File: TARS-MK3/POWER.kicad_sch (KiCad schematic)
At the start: 58 parts, among them J1 Conn_02x12_Odd_Even, J2 Conn_02x12_Odd_Even, J3 Conn_02x12_Odd_Even, J4 Conn_02x12_Odd_Even, J5 AVRISP, U1 LK112M33TR, U2 ATmega328P-A, U3 D36V50F6, U4 D36V50F6, U5 D36V28F9, U6 D36V28F3, U7 D24V50F5, Y1 8Mhz

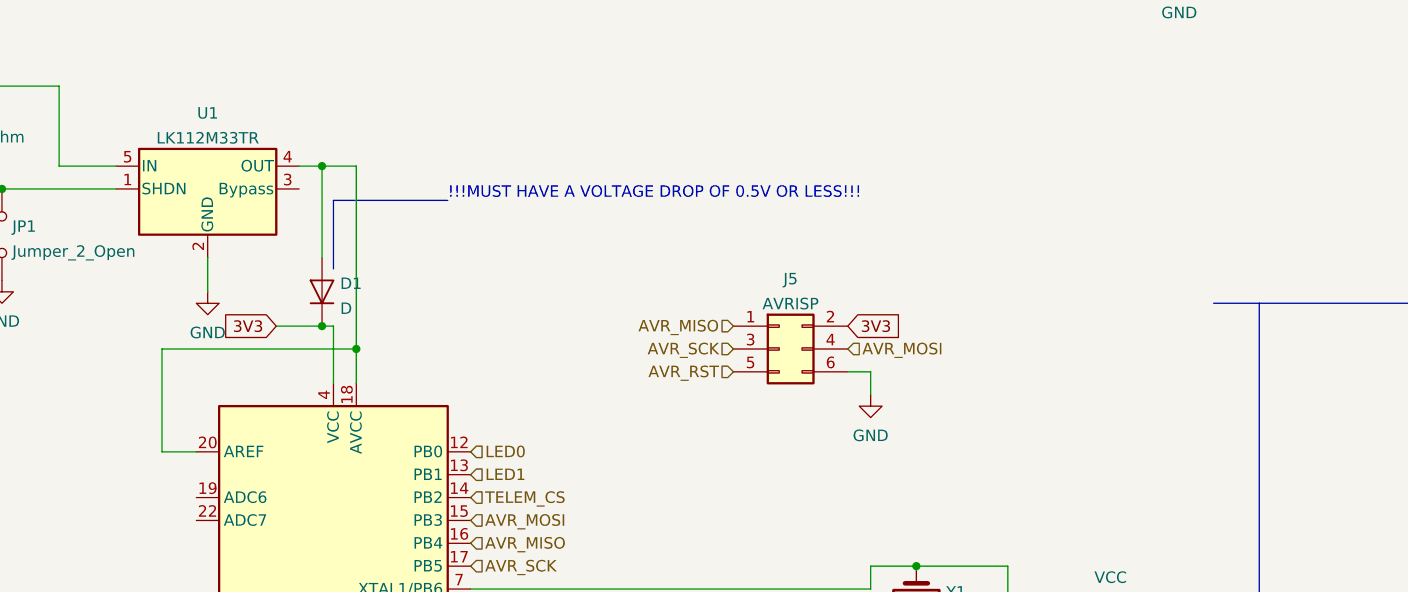
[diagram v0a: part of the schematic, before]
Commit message: Put regulators on PMB and began layout
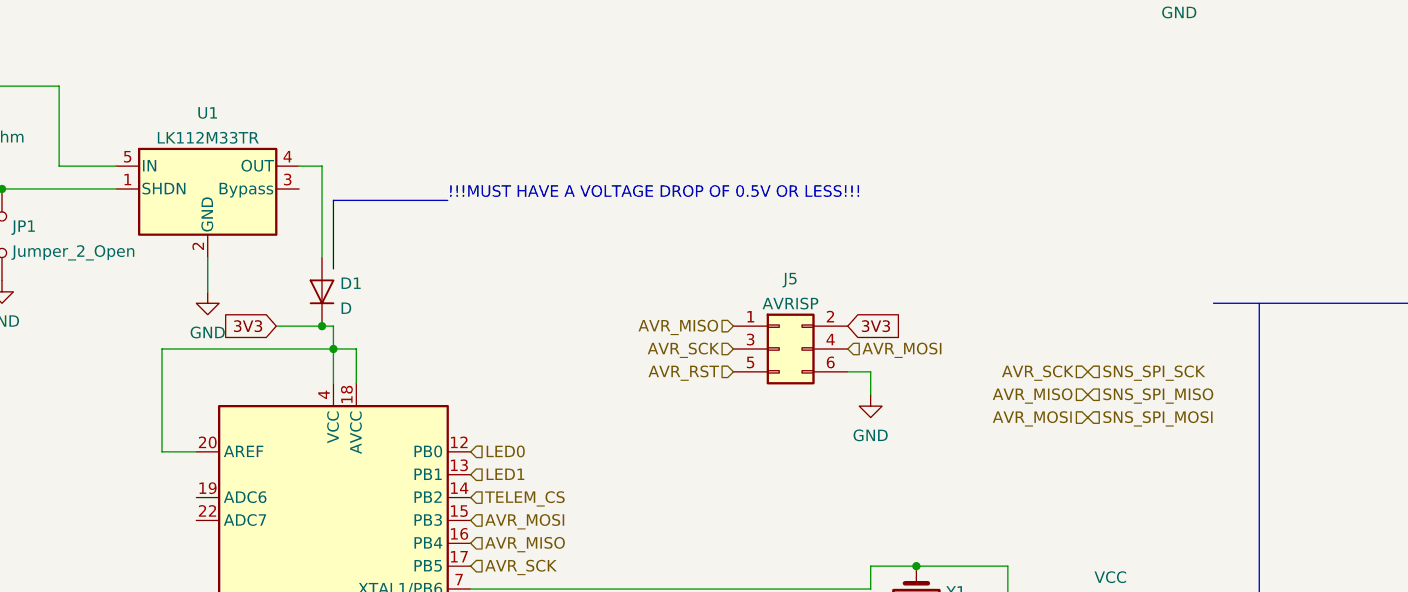
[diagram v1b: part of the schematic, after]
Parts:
- D5: footprint Diode_SMD:D_0603_1608Metric -> Diode_SMD:D_0805_2012Metric
- R18: footprint Resistor_SMD:R_0201_0603Metric -> Resistor_SMD:R_0805_2012Metric
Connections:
- net 3V3: now also U2.18 (AVCC), U2.20 (AREF)
- net at D1.2 (A), U1.4 (OUT): no longer U2.18 (AVCC), U2.20 (AREF)
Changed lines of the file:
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@@
   (junction (at 41.91 176.53) (diameter 0) (color 0 0 0 0)
   )
+  (junction (at 59.69 33.02) (diameter 0) (color 0 0 0 0)
+  )
   (junction (at -33.02 105.41) (diameter 0) (color 0 0 0 0)
   )
@@
   (junction (at 124.46 57.15) (diameter 0) (color 0 0 0 0)
   )
-  (junction (at 58.42 12.7) (diameter 0) (color 0 0 0 0)
-  )
   (junction (at 74.93 184.15) (diameter 0) (color 0 0 0 0)
   )
@@
   )
   (junction (at 58.42 30.48) (diameter 0) (color 0 0 0 0)
-  )
-  (junction (at 62.23 33.02) (diameter 0) (color 0 0 0 0)
   )
   (junction (at 7.62 3.81) (diameter 0) (color 0 0 0 0)
@@
     (stroke (width 0) (type default) (color 0 0 0 0))
   )
-  (wire (pts (xy 62.23 12.7) (xy 62.23 33.02))
-    (stroke (width 0) (type default) (color 0 0 0 0))
-  )
   (wire (pts (xy 69.85 184.15) (xy 69.85 186.69))
     (stroke (width 0) (type default) (color 0 0 0 0))
@@
     (stroke (width 0) (type default) (color 0 0 0 0))
   )
-  (wire (pts (xy 62.23 33.02) (xy 40.64 33.02))
-    (stroke (width 0) (type default) (color 0 0 0 0))
-  )
   (wire (pts (xy 7.62 35.56) (xy 7.62 38.1))
     (stroke (width 0) (type default) (color 0 0 0 0))
@@
     (stroke (width 0) (type default) (color 0 0 0 0))
   )
+  (wire (pts (xy 40.64 33.02) (xy 59.69 33.02))
+    (stroke (width 0) (type default) (color 0 0 0 0))
+  )
   (wire (pts (xy 74.93 90.17) (xy 80.01 90.17))
     (stroke (width 0) (type default) (color 0 0 0 0))
@@
     (stroke (width 0) (type default) (color 0 0 0 0))
   )
-  (wire (pts (xy 59.69 30.48) (xy 59.69 36.83))
+  (wire (pts (xy 59.69 30.48) (xy 59.69 33.02))
     (stroke (width 0) (type default) (color 0 0 0 0))
   )
@@
     (stroke (width 0) (type default) (color 0 0 0 0))
   )
-  (wire (pts (xy 58.42 12.7) (xy 62.23 12.7))
-    (stroke (width 0) (type default) (color 0 0 0 0))
-  )
   (wire (pts (xy -31.75 148.59) (xy -31.75 151.13))
     (stroke (width 0) (type default) (color 0 0 0 0))
@@
     (stroke (width 0) (type default) (color 0 0 0 0))
   )
+  (wire (pts (xy 59.69 33.02) (xy 62.23 33.02))
+    (stroke (width 0) (type default) (color 0 0 0 0))
+  )
   (wire (pts (xy 121.92 72.39) (xy 121.92 73.66))
     (stroke (width 0) (type default) (color 0 0 0 0))
@@
   )
   (wire (pts (xy 92.71 171.45) (xy 90.17 171.45))
+    (stroke (width 0) (type default) (color 0 0 0 0))
+  )
+  (wire (pts (xy 59.69 33.02) (xy 59.69 36.83))
     (stroke (width 0) (type default) (color 0 0 0 0))
   )
@@
     (effects (font (size 1.27 1.27)) (justify left))
   )
+  (hierarchical_label "AVR_MOSI" (shape input) (at 143.51 40.64 180)
+    (effects (font (size 1.27 1.27)) (justify right))
+  )
   (hierarchical_label "B2B_GPIO_21" (shape input) (at 398.78 257.81 0)
     (effects (font (size 1.27 1.27)) (justify left))
@@
     (effects (font (size 1.27 1.27)) (justify left))
   )
+  (hierarchical_label "SNS_SPI_MISO" (shape input) (at 143.51 38.1 0)
+    (effects (font (size 1.27 1.27)) (justify left))
+  )
   (hierarchical_label "TELEM_CS" (shape input) (at 74.93 49.53 0)
     (effects (font (size 1.27 1.27)) (justify left))
@@
     (effects (font (size 1.27 1.27)) (justify left))
   )
+  (hierarchical_label "SNS_SPI_MOSI" (shape input) (at 143.51 40.64 0)
+    (effects (font (size 1.27 1.27)) (justify left))
+  )
   (hierarchical_label "POWER_RESET" (shape input) (at 309.88 285.75 180)
     (effects (font (size 1.27 1.27)) (justify right))
@@
     (effects (font (size 1.27 1.27)) (justify right))
   )
+  (hierarchical_label "SNS_SPI_SCK" (shape input) (at 143.51 35.56 0)
+    (effects (font (size 1.27 1.27)) (justify left))
+  )
   (hierarchical_label "TELEM_RST" (shape input) (at 309.88 280.67 180)
     (effects (font (size 1.27 1.27)) (justify right))
@@
     (effects (font (size 1.27 1.27)) (justify left))
   )
+  (hierarchical_label "AVR_SCK" (shape input) (at 143.51 35.56 180)
+    (effects (font (size 1.27 1.27)) (justify right))
+  )
   (hierarchical_label "B2B_SPI_SCK" (shape input) (at 322.58 288.29 0)
     (effects (font (size 1.27 1.27)) (justify left))
@@
   (hierarchical_label "B2B_UART_SDI" (shape input) (at 80.01 90.17 0)
     (effects (font (size 1.27 1.27)) (justify left))
+  )
+  (hierarchical_label "AVR_MISO" (shape input) (at 143.51 38.1 180)
+    (effects (font (size 1.27 1.27)) (justify right))
   )
   (hierarchical_label "VBAT_MONITOR" (shape input) (at 74.93 67.31 0)
@@
       (effects (font (size 1.27 1.27)) (justify right))
     )
-    (property "Footprint" "Diode_SMD:D_0603_1608Metric" (id 2) (at 212.09 97.79 0)
+    (property "Footprint" "Diode_SMD:D_0805_2012Metric" (id 2) (at 212.09 97.79 0)
       (effects (font (size 1.27 1.27)) hide)
     )
@@
       (effects (font (size 1.27 1.27)) (justify left))
     )
-    (property "Footprint" "Resistor_SMD:R_0201_0603Metric" (id 2) (at 147.066 68.834 90)
+    (property "Footprint" "Resistor_SMD:R_0805_2012Metric" (id 2) (at 147.066 68.834 90)
       (effects (font (size 1.27 1.27)) hide)
     )
@@
     )
     (path "/5ec3bd07-85f5-47e9-a70f-b13f8032dfa2"
-      (reference "D5") (unit 1) (value "LED") (footprint "Diode_SMD:D_0603_1608Metric")
+      (reference "D5") (unit 1) (value "LED") (footprint "Diode_SMD:D_0805_2012Metric")
     )
     (path "/c422545a-de65-4e06-bd9a-ee5945c74c24"
@@
     )
     (path "/623a95d3-92aa-43fc-bfb7-1927169d4600"
-      (reference "R18") (unit 1) (value "10k") (footprint "Resistor_SMD:R_0201_0603Metric")
+      (reference "R18") (unit 1) (value "10k") (footprint "Resistor_SMD:R_0805_2012Metric")
     )
     (path "/6b57d1f0-e39c-4e10-877e-87d046ef1ca7"

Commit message: updated powerboard footprint
updated powerboard footprint
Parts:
- U3, U4: footprint Pololu_regulators:Pololu_6V -> D36V50F6:D36V50F6-TARS
- U5, U6: footprint Pololu_regulators:Pololu_3V3_5V_9V -> D36V28F3:D36V28F3
- U7: footprint Pololu_regulators:Pololu_3V3_5V_9V -> D24V50F5:D24V50F5
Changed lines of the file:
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@@
     (property "Reference" "U5" (id 0) (at 198.12 135.8605 0))
     (property "Value" "D36V28F9" (id 1) (at 198.12 138.6356 0))
-    (property "Footprint" "Pololu_regulators:Pololu_3V3_5V_9V" (id 2) (at 199.39 158.75 0)
+    (property "Footprint" "D36V28F3:D36V28F3" (id 2) (at 199.39 158.75 0)
       (effects (font (size 1.27 1.27)) hide)
     )
@@
     (property "Reference" "U3" (id 0) (at 76.2 128.2405 0))
     (property "Value" "D36V50F6" (id 1) (at 76.2 131.0156 0))
-    (property "Footprint" "Pololu_regulators:Pololu_6V" (id 2) (at 76.2 130.81 0)
+    (property "Footprint" "D36V50F6:D36V50F6-TARS" (id 2) (at 76.2 130.81 0)
       (effects (font (size 1.27 1.27)) hide)
     )
@@
     (property "Reference" "U7" (id 0) (at 227.33 66.04 0))
     (property "Value" "D24V50F5" (id 1) (at 227.33 68.58 0))
-    (property "Footprint" "Pololu_regulators:Pololu_3V3_5V_9V" (id 2) (at 227.33 71.12 0))
+    (property "Footprint" "D24V50F5:D24V50F5" (id 2) (at 227.33 71.12 0))
     (property "Datasheet" "" (id 3) (at 227.33 72.39 0)
       (effects (font (size 1.27 1.27)) hide)
@@
     (property "Reference" "U4" (id 0) (at 76.2 162.5305 0))
     (property "Value" "D36V50F6" (id 1) (at 76.2 165.3056 0))
-    (property "Footprint" "Pololu_regulators:Pololu_6V" (id 2) (at 76.2 165.1 0)
+    (property "Footprint" "D36V50F6:D36V50F6-TARS" (id 2) (at 76.2 165.1 0)
       (effects (font (size 1.27 1.27)) hide)
     )
@@
     (property "Reference" "U6" (id 0) (at 227.33 36.83 0))
     (property "Value" "D36V28F3" (id 1) (at 227.33 39.37 0))
-    (property "Footprint" "Pololu_regulators:Pololu_3V3_5V_9V" (id 2) (at 213.36 54.61 0)
+    (property "Footprint" "D36V28F3:D36V28F3" (id 2) (at 213.36 54.61 0)
       (effects (font (size 1.27 1.27)) hide)
     )
@@
     )
     (path "/3b87441e-9545-4daa-bf5c-0e30f2dd4c01"
-      (reference "U3") (unit 1) (value "D36V50F6") (footprint "Pololu_regulators:Pololu_6V")
+      (reference "U3") (unit 1) (value "D36V50F6") (footprint "D36V50F6:D36V50F6-TARS")
     )
     (path "/d599ee5f-5c96-4c6d-a4f2-87e98db0087b"
-      (reference "U4") (unit 1) (value "D36V50F6") (footprint "Pololu_regulators:Pololu_6V")
+      (reference "U4") (unit 1) (value "D36V50F6") (footprint "D36V50F6:D36V50F6-TARS")
     )
     (path "/100a73e7-13ce-43bc-8783-1b4a2e371823"
-      (reference "U5") (unit 1) (value "D36V28F9") (footprint "Pololu_regulators:Pololu_3V3_5V_9V")
+      (reference "U5") (unit 1) (value "D36V28F9") (footprint "D36V28F3:D36V28F3")
     )
     (path "/fdff5ae7-e28b-42b9-8347-c09e41256987"
-      (reference "U6") (unit 1) (value "D36V28F3") (footprint "Pololu_regulators:Pololu_3V3_5V_9V")
+      (reference "U6") (unit 1) (value "D36V28F3") (footprint "D36V28F3:D36V28F3")
     )
     (path "/60d76cd4-7135-41b5-bb14-f84115e2b595"
-      (reference "U7") (unit 1) (value "D24V50F5") (footprint "Pololu_regulators:Pololu_3V3_5V_9V")
+      (reference "U7") (unit 1) (value "D24V50F5") (footprint "D24V50F5:D24V50F5")
     )
     (path "/dc0ca2fc-3599-4142-ace0-e48580dd6bc3"

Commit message: finished POWER
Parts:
- removed R11: 200kOhm, Resistor_SMD:R_0805_2012Metric, symbol D24V50F5:R_US
- removed R12: 100kOhm, Resistor_SMD:R_0805_2012Metric, symbol D24V50F5:R_US
- D4: footprint Diode_SMD:D_0603_1608Metric -> LED_SMD:LED_0805_2012Metric
- D5: footprint Diode_SMD:D_0805_2012Metric -> LED_SMD:LED_0805_2012Metric
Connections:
- net B2B_GPIO_21 is gone; now on net 6V_AC_SERVO2: J3.24 (Pin_24), J4.23 (Pin_23)
- net B2B_GPIO_4 is gone; now on net 6V_AC_SERVO1: J1.24 (Pin_24), J2.23 (Pin_23)
- net VCC is gone; now on net 3V3: R18.1
- net 3V3_EN: no longer JP4.2 (B)
- net 6V_AC_SERVO1_EN: no longer JP3.2 (B), U2.10 (PD6)
- net 9V_EN: now also JP4.2 (B)
- new net 6V_AC_SERVO2_EN: JP3.2 (B), U2.10 (PD6)

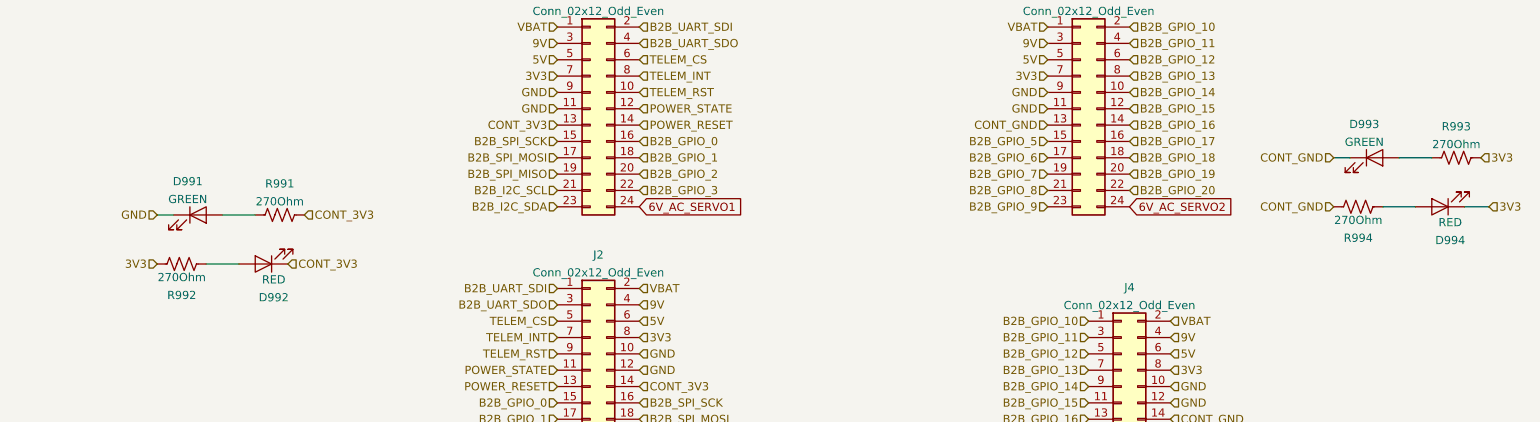
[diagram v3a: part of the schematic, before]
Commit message: Connected continuity check pins correctly on PMB schematic
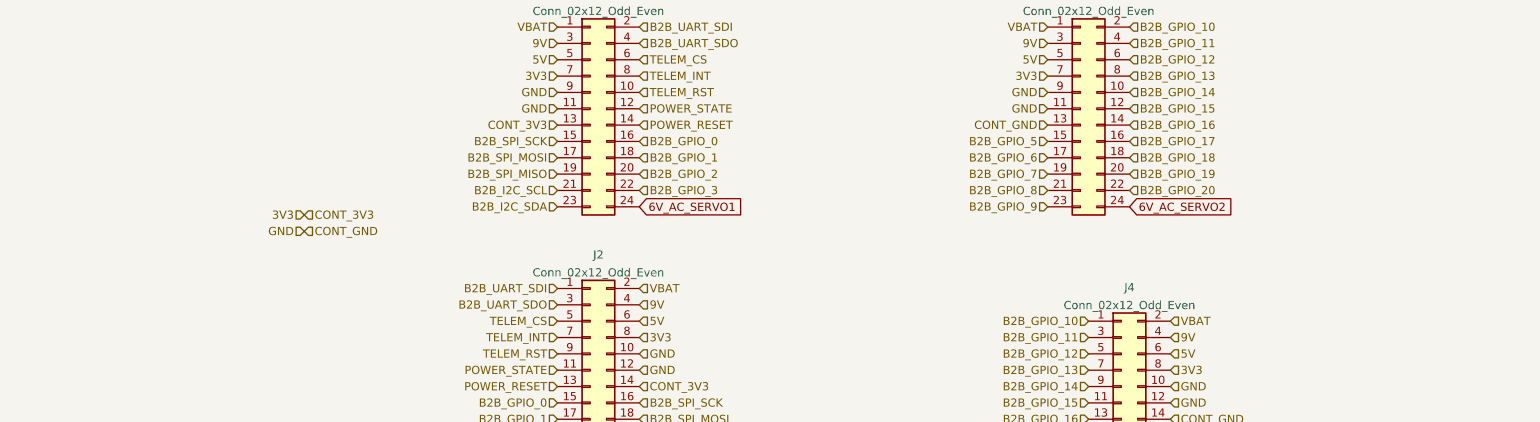
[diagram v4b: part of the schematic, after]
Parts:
- removed D991, D993: GREEN, LED_SMD:LED_0805_2012Metric, symbol D24V50F5:LED
- removed D992, D994: RED, LED_SMD:LED_0805_2012Metric, symbol D24V50F5:LED
- removed R991, R992, R993, R994: 270Ohm, Resistor_SMD:R_0805_2012Metric, symbol D24V50F5:R_US
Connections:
- net CONT_3V3 is gone; now on net 3V3: J1.13 (Pin_13), J2.14 (Pin_14)
- net CONT_GND is gone; now on net GND: J3.13 (Pin_13), J4.14 (Pin_14)
